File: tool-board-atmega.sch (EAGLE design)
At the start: 90 parts, among them IC3 ATMEGA2560-16AU, IC4 ATMEGA8U2-MU, Q1 16MHz, Q2 16MHz, X2 MICROUSB_VERTICAL, Y1 16MHz, Y2 16MHz

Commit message: removed crystals from primary micro
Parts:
- removed C14, C15: 22p, SmartPrj:C-EU0603-RND
- removed Q2: 16MHz, special:XTAL/S
- removed R1: 1M, SmartPrj:R-EU_R0603
- removed R3: 27R, SmartPrj:R-EU_R0603
- removed Y1: 16MHz, SmartPrj:RESONATORMU
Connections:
- removed net XTAL1: C14.2, Q2.2, R1.1, R3.2, Y1.3
- removed net XTAL1R: IC3.XTAL1, R3.1
- removed net XTAL2: C15.2, IC3.XTAL2, Q2.1, R1.2, Y1.1
- net GND: no longer C14.1, C15.1, Y1.2
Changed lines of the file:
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@@
 <part name="UBOOT" library="jumper" deviceset="SJ" device=""/>
 <part name="GROUND" library="jumper" deviceset="SJ" device=""/>
-<part name="Y1" library="SmartPrj" deviceset="RESONATOR" device="MU" value="16MHz"/>
-<part name="GND20" library="supply1" deviceset="GND" device=""/>
-<part name="R1" library="SmartPrj" deviceset="R-EU_" device="R0603" value="1M"/>
 <part name="RN4" library="resistor-dil" deviceset="4R-N" device="CAY16" value="1k"/>
 <part name="RN5" library="resistor-dil" deviceset="4R-N" device="CAT16" value="10K"/>
@@
 <part name="R2" library="SmartPrj" deviceset="R-EU_" device="R0603" value="1M"/>
 <part name="Q1" library="special" deviceset="XTAL/S" device="" value="16MHz"/>
-<part name="Q2" library="special" deviceset="XTAL/S" device="" value="16MHz"/>
-<part name="C14" library="SmartPrj" deviceset="C-EU" device="0603-RND" value="22p"/>
-<part name="C15" library="SmartPrj" deviceset="C-EU" device="0603-RND" value="22p"/>
 <part name="C16" library="SmartPrj" deviceset="C-EU" device="0603-RND" value="22p"/>
 <part name="C17" library="SmartPrj" deviceset="C-EU" device="0603-RND" value="22p"/>
 <part name="GND21" library="supply1" deviceset="GND" device=""/>
-<part name="GND27" library="supply1" deviceset="GND" device=""/>
-<part name="R3" library="SmartPrj" deviceset="R-EU_" device="R0603" value="27R"/>
 <part name="R4" library="SmartPrj" deviceset="R-EU_" device="R0603" value="27R"/>
 <part name="P+2" library="supply1" deviceset="+5V" device=""/>
@@
 <attribute name="VALUE" x="414.02" y="19.05" size="1.778" layer="96"/>
 </instance>
-<instance part="Y1" gate="G$1" x="55.88" y="129.54" smashed="yes">
-<attribute name="NAME" x="50.8" y="134.112" size="1.778" layer="95"/>
-<attribute name="VALUE" x="45.72" y="121.412" size="1.778" layer="96"/>
-</instance>
-<instance part="GND20" gate="1" x="40.64" y="129.54" smashed="yes" rot="R270">
-<attribute name="VALUE" x="38.1" y="132.08" size="1.778" layer="96" rot="R270"/>
-</instance>
-<instance part="R1" gate="G$1" x="27.94" y="129.54" smashed="yes" rot="R90">
-<attribute name="NAME" x="25.4" y="131.2164" size="1.778" layer="95" rot="R180"/>
-<attribute name="VALUE" x="26.035" y="129.032" size="1.778" layer="96" rot="R180"/>
-</instance>
 <instance part="RN4" gate="A" x="482.6" y="2.54" smashed="yes">
 <attribute name="VALUE" x="485.14" y="-0.508" size="1.778" layer="96"/>
@@
 <attribute name="VALUE" x="454.66" y="154.94" size="1.778" layer="96" rot="R90"/>
 </instance>
-<instance part="Q2" gate="G$1" x="467.36" y="160.02" smashed="yes" rot="R90">
-<attribute name="NAME" x="463.55" y="154.94" size="1.778" layer="95" rot="R90"/>
-<attribute name="VALUE" x="472.44" y="154.94" size="1.778" layer="96" rot="R90"/>
-</instance>
-<instance part="C14" gate="G$1" x="492.76" y="165.1" smashed="yes" rot="MR90">
-<attribute name="NAME" x="490.855" y="171.323" size="1.778" layer="95" rot="MR270"/>
-<attribute name="VALUE" x="493.395" y="172.974" size="1.778" layer="96" rot="MR270"/>
-</instance>
-<instance part="C15" gate="G$1" x="492.76" y="154.94" smashed="yes" rot="MR90">
-<attribute name="NAME" x="490.855" y="161.163" size="1.778" layer="95" rot="MR270"/>
-<attribute name="VALUE" x="493.395" y="162.814" size="1.778" layer="96" rot="MR270"/>
-</instance>
 <instance part="C16" gate="G$1" x="429.26" y="165.1" smashed="yes" rot="MR90">
 <attribute name="NAME" x="427.355" y="171.323" size="1.778" layer="95" rot="MR270"/>
@@
 <instance part="GND21" gate="1" x="419.1" y="160.02" smashed="yes" rot="R270">
 <attribute name="VALUE" x="416.56" y="162.56" size="1.778" layer="96" rot="R270"/>
-</instance>
-<instance part="GND27" gate="1" x="500.38" y="160.02" smashed="yes" rot="R90">
-<attribute name="VALUE" x="502.92" y="157.48" size="1.778" layer="96" rot="R90"/>
-</instance>
-<instance part="R3" gate="G$1" x="71.12" y="121.92" smashed="yes" rot="R180">
-<attribute name="NAME" x="69.4436" y="119.38" size="1.778" layer="95" rot="R270"/>
-<attribute name="VALUE" x="71.628" y="120.015" size="1.778" layer="96" rot="R270"/>
 </instance>
 <instance part="R4" gate="G$1" x="421.64" y="66.04" smashed="yes" rot="R180">
@@
 </segment>
 <segment>
-<wire x1="43.18" y1="129.54" x2="48.26" y2="129.54" width="0.1524" layer="91"/>
-<pinref part="Y1" gate="G$1" pin="2"/>
-<pinref part="GND20" gate="1" pin="GND"/>
-</segment>
-<segment>
 <wire x1="424.18" y1="165.1" x2="424.18" y2="160.02" width="0.1524" layer="91"/>
 <wire x1="424.18" y1="160.02" x2="424.18" y2="154.94" width="0.1524" layer="91"/>
@@
 <pinref part="C17" gate="G$1" pin="2"/>
 <pinref part="GND21" gate="1" pin="GND"/>
-</segment>
-<segment>
-<wire x1="495.3" y1="165.1" x2="495.3" y2="160.02" width="0.1524" layer="91"/>
-<wire x1="495.3" y1="160.02" x2="495.3" y2="154.94" width="0.1524" layer="91"/>
-<wire x1="497.84" y1="160.02" x2="495.3" y2="160.02" width="0.1524" layer="91"/>
-<junction x="495.3" y="160.02"/>
-<pinref part="C14" gate="G$1" pin="1"/>
-<pinref part="C15" gate="G$1" pin="1"/>
-<pinref part="GND27" gate="1" pin="GND"/>
 </segment>
 <segment>
@@
 </segment>
 </net>
-<net name="XTAL2" class="0">
-<segment>
-<wire x1="81.28" y1="134.62" x2="88.9" y2="134.62" width="0.1524" layer="91"/>
-<wire x1="88.9" y1="134.62" x2="88.9" y2="132.08" width="0.1524" layer="91"/>
-<wire x1="88.9" y1="132.08" x2="104.14" y2="132.08" width="0.1524" layer="91"/>
-<wire x1="55.88" y1="132.08" x2="55.88" y2="137.16" width="0.1524" layer="91"/>
-<wire x1="55.88" y1="137.16" x2="81.28" y2="137.16" width="0.1524" layer="91"/>
-<wire x1="81.28" y1="137.16" x2="81.28" y2="134.62" width="0.1524" layer="91"/>
-<wire x1="27.94" y1="134.62" x2="27.94" y2="137.16" width="0.1524" layer="91"/>
-<wire x1="27.94" y1="137.16" x2="55.88" y2="137.16" width="0.1524" layer="91"/>
-<junction x="55.88" y="137.16"/>
-<label x="91.44" y="132.08" size="1.778" layer="95"/>
-<pinref part="IC3" gate="1" pin="XTAL2"/>
-<pinref part="Y1" gate="G$1" pin="1"/>
-<pinref part="R1" gate="G$1" pin="2"/>
-</segment>
-<segment>
-<wire x1="467.36" y1="154.94" x2="487.68" y2="154.94" width="0.1524" layer="91"/>
-<label x="477.52" y="154.94" size="1.778" layer="95"/>
-<pinref part="Q2" gate="G$1" pin="1"/>
-<pinref part="C15" gate="G$1" pin="2"/>
-</segment>
-</net>
-<net name="XTAL1" class="0">
-<segment>
-<wire x1="467.36" y1="165.1" x2="487.68" y2="165.1" width="0.1524" layer="91"/>
-<label x="477.52" y="165.1" size="1.778" layer="95"/>
-<pinref part="Q2" gate="G$1" pin="2"/>
-<pinref part="C14" gate="G$1" pin="2"/>
-</segment>
-<segment>
-<wire x1="66.04" y1="121.92" x2="60.96" y2="121.92" width="0.1524" layer="91"/>
-<wire x1="60.96" y1="121.92" x2="60.96" y2="116.84" width="0.1524" layer="91"/>
-<wire x1="60.96" y1="116.84" x2="55.88" y2="116.84" width="0.1524" layer="91"/>
-<wire x1="55.88" y1="116.84" x2="55.88" y2="127" width="0.1524" layer="91"/>
-<wire x1="55.88" y1="116.84" x2="27.94" y2="116.84" width="0.1524" layer="91"/>
-<wire x1="27.94" y1="116.84" x2="27.94" y2="124.46" width="0.1524" layer="91"/>
-<junction x="55.88" y="116.84"/>
-<label x="60.96" y="121.92" size="1.778" layer="95"/>
-<pinref part="R1" gate="G$1" pin="1"/>
-<pinref part="Y1" gate="G$1" pin="3"/>
-<pinref part="R3" gate="G$1" pin="2"/>
-</segment>
-</net>
 <net name="XT2" class="0">
 <segment>
@@
 </segment>
 </net>
-<net name="XTAL1R" class="0">
-<segment>
-<wire x1="104.14" y1="127" x2="88.9" y2="127" width="0.1524" layer="91"/>
-<wire x1="88.9" y1="127" x2="88.9" y2="124.46" width="0.1524" layer="91"/>
-<wire x1="88.9" y1="124.46" x2="81.28" y2="124.46" width="0.1524" layer="91"/>
-<wire x1="81.28" y1="124.46" x2="81.28" y2="121.92" width="0.1524" layer="91"/>
-<wire x1="76.2" y1="121.92" x2="81.28" y2="121.92" width="0.1524" layer="91"/>
-<label x="91.44" y="127" size="1.778" layer="95"/>
-<pinref part="IC3" gate="1" pin="XTAL1"/>
-<pinref part="R3" gate="G$1" pin="1"/>
-</segment>
-</net>

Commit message: changed LEDs and Diodes to all be 0603 package
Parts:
- R15: device SmartPrj:R-EU_R0603 -> tool-board-atmega:SMARTPRJ_R-EU_0603-RND
- U$16, U$17: value DIODE0805 -> 0603DIODE; device ClinicalRobotics:DIODE0805 -> ClinicalRobotics:0603DIODE
- U$20, U$21: value 0805LED -> 0603LED; device ClinicalRobotics:0805LED -> ClinicalRobotics:0603LED
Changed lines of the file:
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@@
 <layer number="254" name="cooling" color="7" fill="1" visible="no" active="yes"/>
 </layers>
-<schematic>
+<schematic xreflabel="%F%N/%S.%C%R" xrefpart="/%S.%C%R">
 <attributes>
 </attributes>
@@
 <part name="R11" library="SmartPrj" deviceset="R-EU_" device="R0603" value="56"/>
 <part name="R12" library="SmartPrj" deviceset="R-EU_" device="R0603" value="22"/>
-<part name="U$16" library="ClinicalRobotics" deviceset="DIODE0805" device=""/>
-<part name="U$17" library="ClinicalRobotics" deviceset="DIODE0805" device=""/>
+<part name="U$16" library="ClinicalRobotics" deviceset="0603DIODE" device=""/>
+<part name="U$17" library="ClinicalRobotics" deviceset="0603DIODE" device=""/>
 <part name="DBG" library="con-molex" library_urn="urn:adsk.eagle:library:165" deviceset="22-23-2101" device="" package3d_urn="urn:adsk.eagle:package:8078641/1"/>
 <part name="GND19" library="supply1" deviceset="GND" device=""/>
@@
 <part name="P+19" library="supply1" deviceset="+5V" device=""/>
 <part name="U$19" library="ClinicalRobotics" deviceset="0805LED" device=""/>
-<part name="U$20" library="ClinicalRobotics" deviceset="0805LED" device=""/>
-<part name="U$21" library="ClinicalRobotics" deviceset="0805LED" device=""/>
+<part name="U$20" library="ClinicalRobotics" deviceset="0603LED" device=""/>
+<part name="U$21" library="ClinicalRobotics" deviceset="0603LED" device=""/>
 <part name="RN8" library="resistor-dil" library_urn="urn:adsk.eagle:library:342" deviceset="4R-N" device="CAY16" package3d_urn="urn:adsk.eagle:package:24918/1"/>
 <part name="P+20" library="supply1" deviceset="+5V" device=""/>
 <part name="R13" library="SmartPrj" deviceset="R-EU_" device="R0603" value="1M"/>
 <part name="R14" library="SmartPrj" deviceset="R-EU_" device="R0603" value="100"/>
-<part name="R15" library="SmartPrj" deviceset="R-EU_" device="R0603" value="1M"/>
+<part name="R15" library="tool-board-atmega" deviceset="SMARTPRJ_R-EU_" device="0603-RND" value="1M"/>
 <part name="R16" library="SmartPrj" deviceset="R-EU_" device="R0603" value="100"/>
 <part name="GND13" library="supply1" deviceset="GND" device=""/>

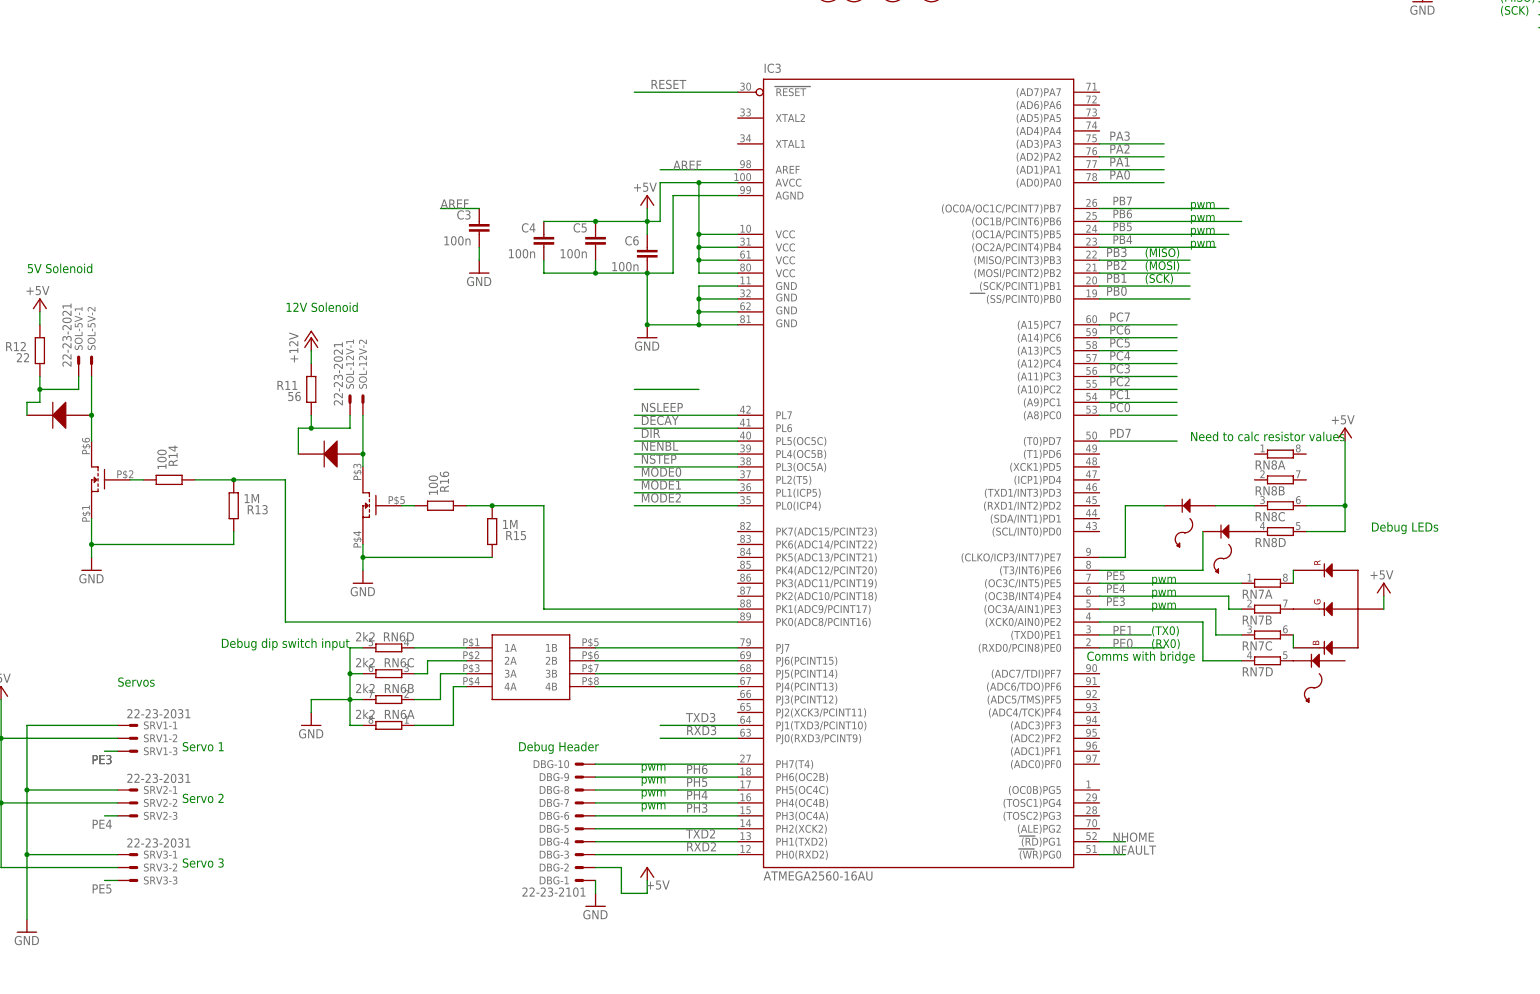
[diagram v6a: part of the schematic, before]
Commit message: placed all components, made Servo connectors 4 pin
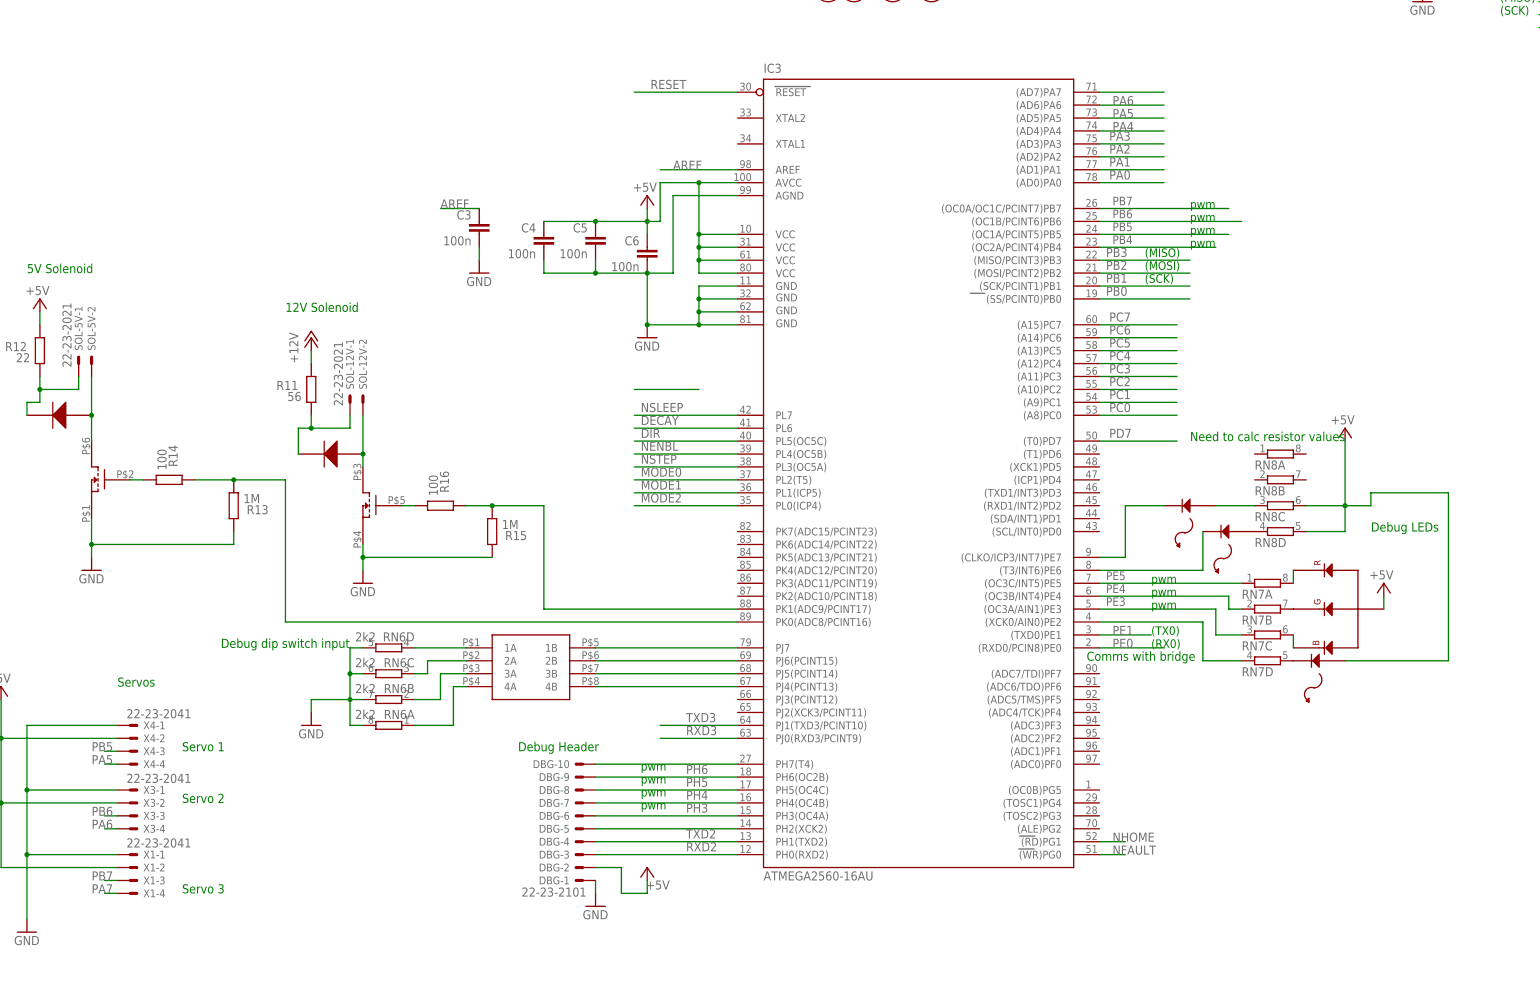
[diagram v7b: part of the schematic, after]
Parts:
- removed SRV1, SRV2, SRV3: 22-23-2031, con-molex:22-23-2031
- added X1, X3, X4: 22-23-2041, con-molex:22-23-2041
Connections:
- new net PA4: IC3.(AD4)PA4
- new net PA5: IC3.(AD5)PA5, X4-4.S
- new net PA6: IC3.(AD6)PA6, X3-4.S
- new net PA7: IC3.(AD7)PA7, X1-4.S
- net +5V: now also U$19.A, X1-2.S, X3-2.S, X4-2.S; no longer SRV1-2.S, SRV2-2.S, SRV3-2.S
- net GND: now also X1-1.S, X3-1.S, X4-1.S; no longer SRV1-1.S, SRV2-1.S, SRV3-1.S
- net PB5: now also X4-3.S
- net PB6: now also X3-3.S
- net PB7: now also X1-3.S
- net PE3: no longer SRV1-3.S
- net PE4: no longer SRV2-3.S
- net PE5: no longer SRV3-3.S
